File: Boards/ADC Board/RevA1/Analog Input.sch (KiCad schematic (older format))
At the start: 1 part, among them J14 Screw Terminals

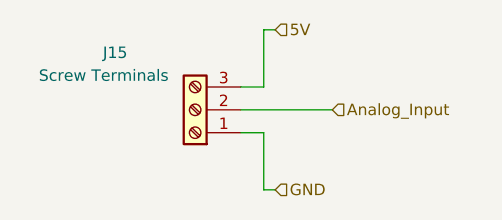
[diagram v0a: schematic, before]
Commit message: Added 12-pin and 4-pin spring terminal footprints. Updated footprints for ADC board. Continued work on PCB layout of ADC board.
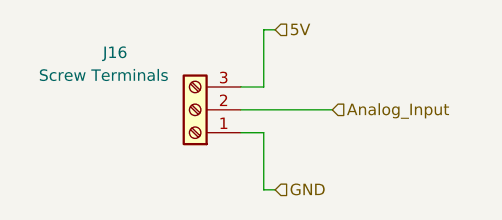
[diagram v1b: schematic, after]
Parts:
- J14: footprint Connector_PinHeader_2.54mm:PinHeader_1x03_P2.54mm_Vertical -> footprints:1985292
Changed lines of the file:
@@
 $Descr A4 11693 8268
 encoding utf-8
-Sheet 8 11
+Sheet 9 11
 Title ""
 Date ""
@@
 AR Path="/61657053/61653B35" Ref="J16"  Part="1"
 AR Path="/616571E9/61653B35" Ref="J17"  Part="1"
-F 0 "J15" H 2000 1050 50  0000 C CNN
+F 0 "J16" H 2000 1050 50  0000 C CNN
 F 1 "Screw Terminals" H 2050 1150 50  0000 C CNN
-F 2 "Connector_PinHeader_2.54mm:PinHeader_1x03_P2.54mm_Vertical" H 1650 1300 50  0001 C CNN
+F 2 "footprints:1985292" H 1650 1300 50  0001 C CNN
 F 3 "~" H 1650 1300 50  0001 C CNN
 	1    1650 1300

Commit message: Imported 4 pin spring terminals. Replaced 12 pin terminals with 4 pin terminals on ADC board. Placed 4 pin terminals on PCB.
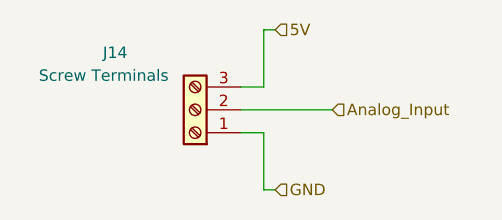
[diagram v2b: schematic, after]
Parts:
- J14: footprint footprints:1985292 -> Spring_Terminal_4Pin:1984989
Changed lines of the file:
@@
 $Descr A4 11693 8268
 encoding utf-8
-Sheet 9 11
+Sheet 7 11
 Title ""
 Date ""
@@
 AR Path="/61657053/61653B35" Ref="J16"  Part="1"
 AR Path="/616571E9/61653B35" Ref="J17"  Part="1"
-F 0 "J16" H 2000 1050 50  0000 C CNN
+F 0 "J14" H 2000 1050 50  0000 C CNN
 F 1 "Screw Terminals" H 2050 1150 50  0000 C CNN
-F 2 "footprints:1985292" H 1650 1300 50  0001 C CNN
+F 2 "Spring_Terminal_4Pin:1984989" H 1650 1300 50  0001 C CNN
 F 3 "~" H 1650 1300 50  0001 C CNN
 	1    1650 1300

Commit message: Created and layed out most of PCB for microvolt board. Removed one strain module, and added multiple mounting holes for the boards to be placed on.
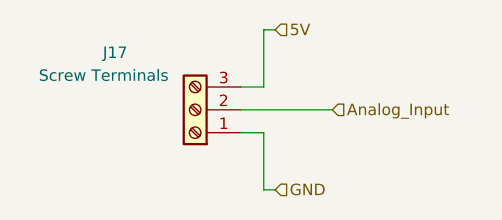
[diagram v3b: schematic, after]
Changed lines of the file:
@@
 $Descr A4 11693 8268
 encoding utf-8
-Sheet 7 11
+Sheet 10 11
 Title ""
 Date ""
@@
 AR Path="/61657053/61653B35" Ref="J16"  Part="1"
 AR Path="/616571E9/61653B35" Ref="J17"  Part="1"
-F 0 "J14" H 2000 1050 50  0000 C CNN
+F 0 "J17" H 2000 1050 50  0000 C CNN
 F 1 "Screw Terminals" H 2050 1150 50  0000 C CNN
 F 2 "Spring_Terminal_4Pin:1984989" H 1650 1300 50  0001 C CNN
